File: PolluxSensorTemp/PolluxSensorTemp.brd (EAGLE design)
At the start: 100 x 80 mm, 0 parts

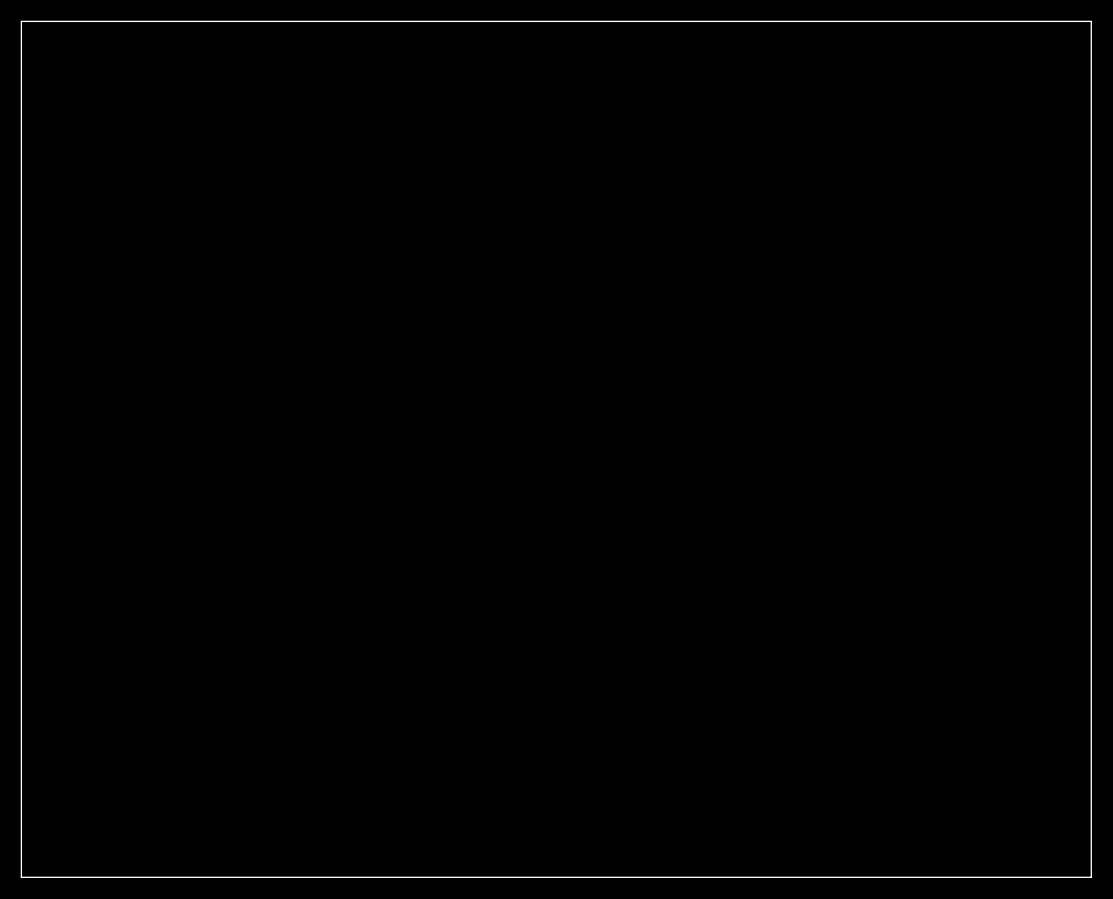
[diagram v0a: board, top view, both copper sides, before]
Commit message: add Temp sensor board and schematics
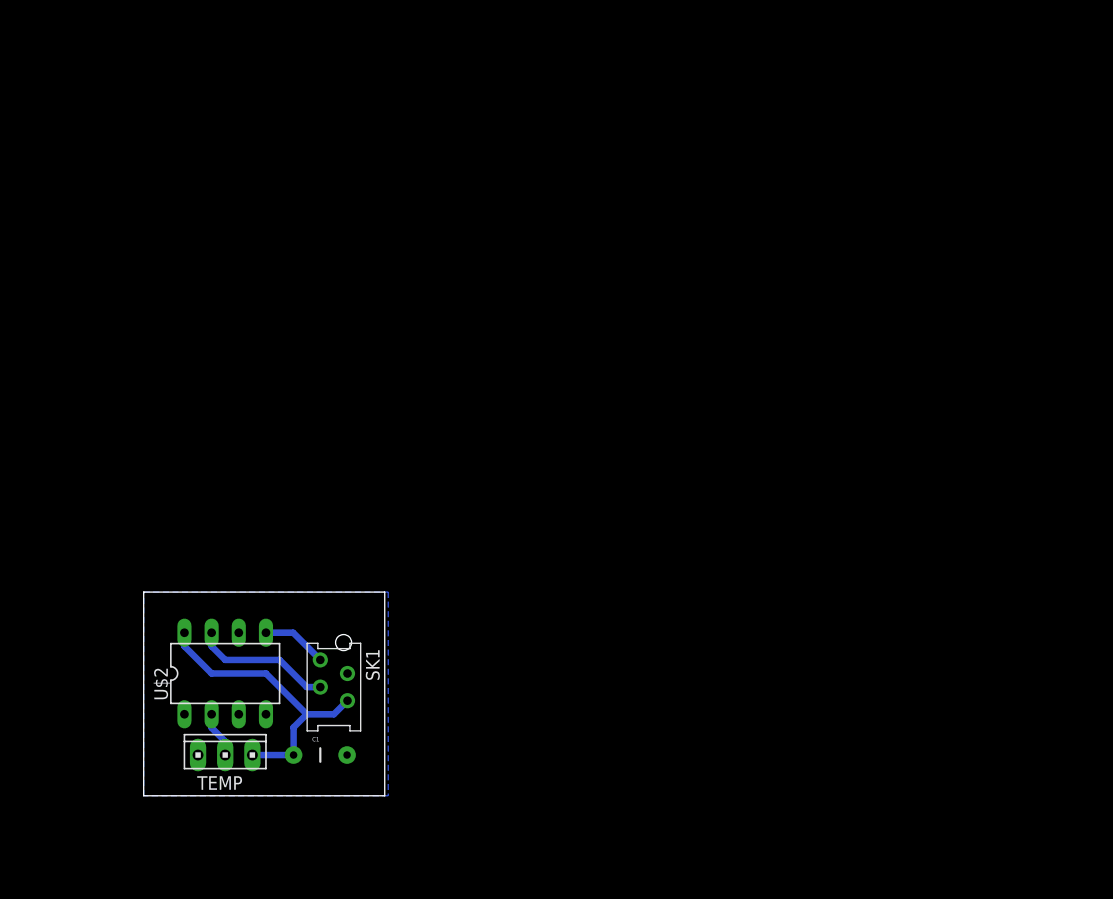
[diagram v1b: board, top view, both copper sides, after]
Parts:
- added C1: (no value), SparkFun:CAP-PTH-5MM
- added SK1: (no value), jt-con-micromatch:AMP-215079-8
- added TEMP: (no value), con-amp:10X03MTA
- added U$2: TINY25/45/85-20PU, avr-7:DIL08
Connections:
- new net 5V: C1.1, SK1.4, TEMP.1, U$2.8
- new net GND: C1.2, SK1.2, TEMP.3, U$2.4
- new net N$1: SK1.3, U$2.7
- new net N$2: SK1.1, U$2.5
- new net READ: TEMP.2, U$2.2
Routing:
- net 5V: track 0.00 -> 27.8 mm
- net N$1: track 0.00 -> 13.0 mm
- net N$2: track 0.00 -> 6.13 mm
- net READ: track 0.00 -> 4.34 mm
- added copper zone on layer 16, net GND
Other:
- board size 100 x 80 mm -> 22.5 x 19 mm
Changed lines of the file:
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@@
 <board>
 <plain>
-<wire x1="0" y1="0" x2="100" y2="0" width="0" layer="20"/>
-<wire x1="100" y1="0" x2="100" y2="80" width="0" layer="20"/>
-<wire x1="100" y1="80" x2="0" y2="80" width="0" layer="20"/>
-<wire x1="0" y1="80" x2="0" y2="0" width="0" layer="20"/>
+<wire x1="11.43" y1="7.62" x2="33.96" y2="7.62" width="0" layer="20"/>
+<wire x1="33.96" y1="7.62" x2="33.96" y2="26.66" width="0" layer="20"/>
+<wire x1="33.96" y1="26.66" x2="11.43" y2="26.66" width="0" layer="20"/>
+<wire x1="11.43" y1="26.66" x2="11.43" y2="7.62" width="0" layer="20"/>
 </plain>
 <attributes>
@@
 <param name="mtCopper" value="0.035mm 0.035mm 0.035mm 0.035mm 0.035mm 0.035mm 0.035mm 0.035mm 0.035mm 0.035mm 0.035mm 0.035mm 0.035mm 0.035mm 0.035mm 0.035mm"/>
 <param name="mtIsolate" value="1.5mm 0.15mm 0.2mm 0.15mm 0.2mm 0.15mm 0.2mm 0.15mm 0.2mm 0.15mm 0.2mm 0.15mm 0.2mm 0.15mm 0.2mm"/>
-<param name="mdWireWire" value="8mil"/>
-<param name="mdWirePad" value="8mil"/>
-<param name="mdWireVia" value="8mil"/>
+<param name="mdWireWire" value="24mil"/>
+<param name="mdWirePad" value="24mil"/>
+<param name="mdWireVia" value="24mil"/>
 <param name="mdPadPad" value="8mil"/>
 <param name="mdPadVia" value="8mil"/>
@@
 <param name="mdDrill" value="8mil"/>
 <param name="mdSmdStop" value="0mil"/>
-<param name="msWidth" value="10mil"/>
+<param name="msWidth" value="24mil"/>
 <param name="msDrill" value="24mil"/>
 <param name="msMicroVia" value="9.99mm"/>
@@
 </autorouter>
 <elements>
+<element name="SK1" library="jt-con-micromatch" package="AMP-215079-8" value="" x="29.21" y="20.32" rot="R270"/>
+<element name="U$2" library="avr-7" package="DIL08" value="TINY25/45/85-20PU" x="19.05" y="19.05"/>
+<element name="TEMP" library="con-amp" package="10X03MTA" value="" x="19.05" y="11.43"/>
+<element name="C1" library="SparkFun" package="CAP-PTH-5MM" value="" x="27.94" y="11.43"/>
 </elements>
 <signals>
+<signal name="N$2">
+<contactref element="SK1" pad="1"/>
+<contactref element="U$2" pad="5"/>
+<wire x1="22.86" y1="22.86" x2="25.4" y2="22.86" width="0.6096" layer="16"/>
+<wire x1="25.4" y1="22.86" x2="27.94" y2="20.32" width="0.6096" layer="16"/>
+</signal>
+<signal name="5V">
+<contactref element="SK1" pad="4"/>
+<contactref element="U$2" pad="8"/>
+<contactref element="C1" pad="1"/>
+<contactref element="TEMP" pad="1"/>
+<wire x1="21.59" y1="11.43" x2="25.44" y2="11.43" width="0.6096" layer="16"/>
+<wire x1="15.24" y1="22.86" x2="15.24" y2="21.59" width="0.6096" layer="16"/>
+<wire x1="15.24" y1="21.59" x2="17.78" y2="19.05" width="0.6096" layer="16"/>
+<wire x1="17.78" y1="19.05" x2="22.86" y2="19.05" width="0.6096" layer="16"/>
+<wire x1="22.86" y1="19.05" x2="26.67" y2="15.24" width="0.6096" layer="16"/>
+<wire x1="26.67" y1="15.24" x2="29.21" y2="15.24" width="0.6096" layer="16"/>
+<wire x1="29.21" y1="15.24" x2="30.48" y2="16.51" width="0.6096" layer="16"/>
+<wire x1="25.44" y1="11.43" x2="25.44" y2="14.01" width="0.6096" layer="16"/>
+<wire x1="25.44" y1="14.01" x2="26.67" y2="15.24" width="0.6096" layer="16"/>
+</signal>
+<signal name="GND">
+<contactref element="U$2" pad="4"/>
+<contactref element="SK1" pad="2"/>
+<polygon width="0.4064" layer="16" orphans="yes">
+<vertex x="11.43" y="26.67"/>
+<vertex x="34.29" y="26.67"/>
+<vertex x="34.29" y="7.62"/>
+<vertex x="11.43" y="7.62"/>
+</polygon>
+<contactref element="TEMP" pad="3"/>
+<contactref element="C1" pad="2"/>
+</signal>
+<signal name="N$1">
+<contactref element="U$2" pad="7"/>
+<contactref element="SK1" pad="3"/>
+<wire x1="17.78" y1="22.86" x2="17.78" y2="21.59" width="0.6096" layer="16"/>
+<wire x1="17.78" y1="21.59" x2="19.05" y2="20.32" width="0.6096" layer="16"/>
+<wire x1="19.05" y1="20.32" x2="24.13" y2="20.32" width="0.6096" layer="16"/>
+<wire x1="24.13" y1="20.32" x2="26.67" y2="17.78" width="0.6096" layer="16"/>
+<wire x1="26.67" y1="17.78" x2="27.94" y2="17.78" width="0.6096" layer="16"/>
+</signal>
+<signal name="READ">
+<contactref element="U$2" pad="2"/>
+<contactref element="TEMP" pad="2"/>
+<wire x1="17.78" y1="15.24" x2="17.78" y2="13.97" width="0.6096" layer="16"/>
+<wire x1="17.78" y1="13.97" x2="19.05" y2="12.7" width="0.6096" layer="16"/>
+<wire x1="19.05" y1="12.7" x2="19.05" y2="11.43" width="0.6096" layer="16"/>
+</signal>
 </signals>
 </board>

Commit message: improve sensor board
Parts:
- removed SK1: (no value), jt-con-micromatch:AMP-215079-8
- added C2: 1 uF, SparkFun:CPOL-RADIAL-10UF-25V
- added SK2: (no value), jt-con-micromatch:AMP-215079-8
- C1: value (none) -> 10 pF
- moved C1 13.7 mm to (15.2, 16.5), turned to 180 degrees
- moved U$2 6.48 mm to (25.4, 20.3)
- moved TEMP 5.24 mm to (24.1, 12.7), turned to 180 degrees
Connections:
- removed net N$2: SK1.1, U$2.5
- new net SDA: SK2.4, U$2.5
- net 5V: now also C2.1, SK2.1; no longer SK1.4
- net GND: now also C2.2, SK2.2; no longer SK1.2
- net N$1: now also SK2.3; no longer SK1.3
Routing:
- net SDA: track 0.00 -> 17.3 mm
- net 5V: track 27.8 -> 18.3 mm
- net N$2: track 6.13 -> 0.00 mm
- net N$1: track 13.0 -> 9.94 mm
- net READ: track 4.34 -> 3.81 mm
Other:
- board size 22.5 x 19 mm -> 21.3 x 20.3 mm
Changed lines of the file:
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@@
 <layer number="43" name="vRestrict" color="2" fill="10" visible="yes" active="yes"/>
 <layer number="44" name="Drills" color="7" fill="1" visible="no" active="yes"/>
-<layer number="45" name="Holes" color="7" fill="1" visible="no" active="yes"/>
+<layer number="45" name="Holes" color="7" fill="1" visible="yes" active="yes"/>
 <layer number="46" name="Milling" color="3" fill="1" visible="no" active="yes"/>
 <layer number="47" name="Measures" color="7" fill="1" visible="no" active="yes"/>
@@
 <board>
 <plain>
-<wire x1="11.43" y1="7.62" x2="33.96" y2="7.62" width="0" layer="20"/>
-<wire x1="33.96" y1="7.62" x2="33.96" y2="26.66" width="0" layer="20"/>
-<wire x1="33.96" y1="26.66" x2="11.43" y2="26.66" width="0" layer="20"/>
-<wire x1="11.43" y1="26.66" x2="11.43" y2="7.62" width="0" layer="20"/>
+<wire x1="11.43" y1="8.89" x2="32.69" y2="8.89" width="0" layer="20"/>
+<wire x1="32.69" y1="8.89" x2="32.69" y2="29.2" width="0" layer="20"/>
+<wire x1="32.69" y1="29.2" x2="11.43" y2="29.2" width="0" layer="20"/>
+<wire x1="11.43" y1="29.2" x2="11.43" y2="8.89" width="0" layer="20"/>
+<hole x="12.7" y="27.94" drill="1.5"/>
+<hole x="12.7" y="10.16" drill="1.5"/>
+<hole x="31.75" y="10.16" drill="1.5"/>
+<hole x="31.75" y="27.94" drill="1.5"/>
 </plain>
 <attributes>
@@
 </autorouter>
 <elements>
-<element name="SK1" library="jt-con-micromatch" package="AMP-215079-8" value="" x="29.21" y="20.32" rot="R270"/>
-<element name="U$2" library="avr-7" package="DIL08" value="TINY25/45/85-20PU" x="19.05" y="19.05"/>
-<element name="TEMP" library="con-amp" package="10X03MTA" value="" x="19.05" y="11.43"/>
-<element name="C1" library="SparkFun" package="CAP-PTH-5MM" value="" x="27.94" y="11.43"/>
+<element name="U$2" library="avr-7" package="DIL08" value="TINY25/45/85-20PU" x="25.4" y="20.32"/>
+<element name="TEMP" library="con-amp" package="10X03MTA" value="" x="24.13" y="12.7" rot="R180"/>
+<element name="C1" library="SparkFun" package="CAP-PTH-5MM" value="10 pF" x="15.24" y="16.51" rot="R180"/>
+<element name="SK2" library="jt-con-micromatch" package="AMP-215079-8" value="" x="16.51" y="21.59" rot="R90"/>
+<element name="C2" library="SparkFun" package="CPOL-RADIAL-10UF-25V" value="1 uF" x="16.51" y="12.7"/>
 </elements>
 <signals>
-<signal name="N$2">
-<contactref element="SK1" pad="1"/>
-<contactref element="U$2" pad="5"/>
-<wire x1="22.86" y1="22.86" x2="25.4" y2="22.86" width="0.6096" layer="16"/>
-<wire x1="25.4" y1="22.86" x2="27.94" y2="20.32" width="0.6096" layer="16"/>
-</signal>
 <signal name="5V">
-<contactref element="SK1" pad="4"/>
 <contactref element="U$2" pad="8"/>
 <contactref element="C1" pad="1"/>
 <contactref element="TEMP" pad="1"/>
-<wire x1="21.59" y1="11.43" x2="25.44" y2="11.43" width="0.6096" layer="16"/>
-<wire x1="15.24" y1="22.86" x2="15.24" y2="21.59" width="0.6096" layer="16"/>
-<wire x1="15.24" y1="21.59" x2="17.78" y2="19.05" width="0.6096" layer="16"/>
-<wire x1="17.78" y1="19.05" x2="22.86" y2="19.05" width="0.6096" layer="16"/>
-<wire x1="22.86" y1="19.05" x2="26.67" y2="15.24" width="0.6096" layer="16"/>
-<wire x1="26.67" y1="15.24" x2="29.21" y2="15.24" width="0.6096" layer="16"/>
-<wire x1="29.21" y1="15.24" x2="30.48" y2="16.51" width="0.6096" layer="16"/>
-<wire x1="25.44" y1="11.43" x2="25.44" y2="14.01" width="0.6096" layer="16"/>
-<wire x1="25.44" y1="14.01" x2="26.67" y2="15.24" width="0.6096" layer="16"/>
+<contactref element="SK2" pad="1"/>
+<contactref element="C2" pad="1"/>
+<wire x1="17.78" y1="21.59" x2="20.32" y2="21.59" width="0.6096" layer="16"/>
+<wire x1="20.32" y1="21.59" x2="21.59" y2="22.86" width="0.6096" layer="16"/>
+<wire x1="21.59" y1="22.86" x2="21.59" y2="24.13" width="0.6096" layer="16"/>
+<wire x1="17.78" y1="21.59" x2="17.78" y2="16.51" width="0.6096" layer="16"/>
+<wire x1="17.78" y1="16.51" x2="17.74" y2="16.51" width="0.6096" layer="16"/>
+<wire x1="17.78" y1="16.51" x2="17.78" y2="12.7" width="0.6096" layer="16"/>
+<wire x1="17.78" y1="12.7" x2="21.59" y2="12.7" width="0.6096" layer="16"/>
 </signal>
 <signal name="GND">
 <contactref element="U$2" pad="4"/>
-<contactref element="SK1" pad="2"/>
 <polygon width="0.4064" layer="16" orphans="yes">
-<vertex x="11.43" y="26.67"/>
-<vertex x="34.29" y="26.67"/>
-<vertex x="34.29" y="7.62"/>
-<vertex x="11.43" y="7.62"/>
+<vertex x="11.43" y="29.21"/>
+<vertex x="33.02" y="29.21"/>
+<vertex x="33.02" y="8.89"/>
+<vertex x="11.43" y="8.89"/>
 </polygon>
 <contactref element="TEMP" pad="3"/>
 <contactref element="C1" pad="2"/>
+<contactref element="C2" pad="2"/>
+<contactref element="SK2" pad="2"/>
 </signal>
 <signal name="N$1">
 <contactref element="U$2" pad="7"/>
-<contactref element="SK1" pad="3"/>
-<wire x1="17.78" y1="22.86" x2="17.78" y2="21.59" width="0.6096" layer="16"/>
-<wire x1="17.78" y1="21.59" x2="19.05" y2="20.32" width="0.6096" layer="16"/>
-<wire x1="19.05" y1="20.32" x2="24.13" y2="20.32" width="0.6096" layer="16"/>
-<wire x1="24.13" y1="20.32" x2="26.67" y2="17.78" width="0.6096" layer="16"/>
-<wire x1="26.67" y1="17.78" x2="27.94" y2="17.78" width="0.6096" layer="16"/>
+<contactref element="SK2" pad="3"/>
+<wire x1="17.78" y1="24.13" x2="17.78" y2="25.4" width="0.6096" layer="16"/>
+<wire x1="17.78" y1="25.4" x2="19.05" y2="26.67" width="0.6096" layer="16"/>
+<wire x1="19.05" y1="26.67" x2="22.86" y2="26.67" width="0.6096" layer="16"/>
+<wire x1="22.86" y1="26.67" x2="24.13" y2="25.4" width="0.6096" layer="16"/>
+<wire x1="24.13" y1="25.4" x2="24.13" y2="24.13" width="0.6096" layer="16"/>
 </signal>
 <signal name="READ">
 <contactref element="U$2" pad="2"/>
 <contactref element="TEMP" pad="2"/>
-<wire x1="17.78" y1="15.24" x2="17.78" y2="13.97" width="0.6096" layer="16"/>
-<wire x1="17.78" y1="13.97" x2="19.05" y2="12.7" width="0.6096" layer="16"/>
-<wire x1="19.05" y1="12.7" x2="19.05" y2="11.43" width="0.6096" layer="16"/>
+<wire x1="24.13" y1="12.7" x2="24.13" y2="16.51" width="0.6096" layer="16"/>
+</signal>
+<signal name="SDA">
+<contactref element="U$2" pad="5"/>
+<contactref element="SK2" pad="4"/>
+<wire x1="15.24" y1="25.4" x2="17.78" y2="27.94" width="0.6096" layer="16"/>
+<wire x1="17.78" y1="27.94" x2="26.67" y2="27.94" width="0.6096" layer="16"/>
+<wire x1="26.67" y1="27.94" x2="29.21" y2="25.4" width="0.6096" layer="16"/>
+<wire x1="29.21" y1="25.4" x2="29.21" y2="24.13" width="0.6096" layer="16"/>
 </signal>
 </signals>
